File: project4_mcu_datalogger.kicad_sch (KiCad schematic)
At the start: 25 parts, among them U1 24LC1025, U2 24LC1025, U3 ATMEGA328P-AU, U4 DS1337S_T_R, Y1 32.768 KHz, Y2 16 MHz

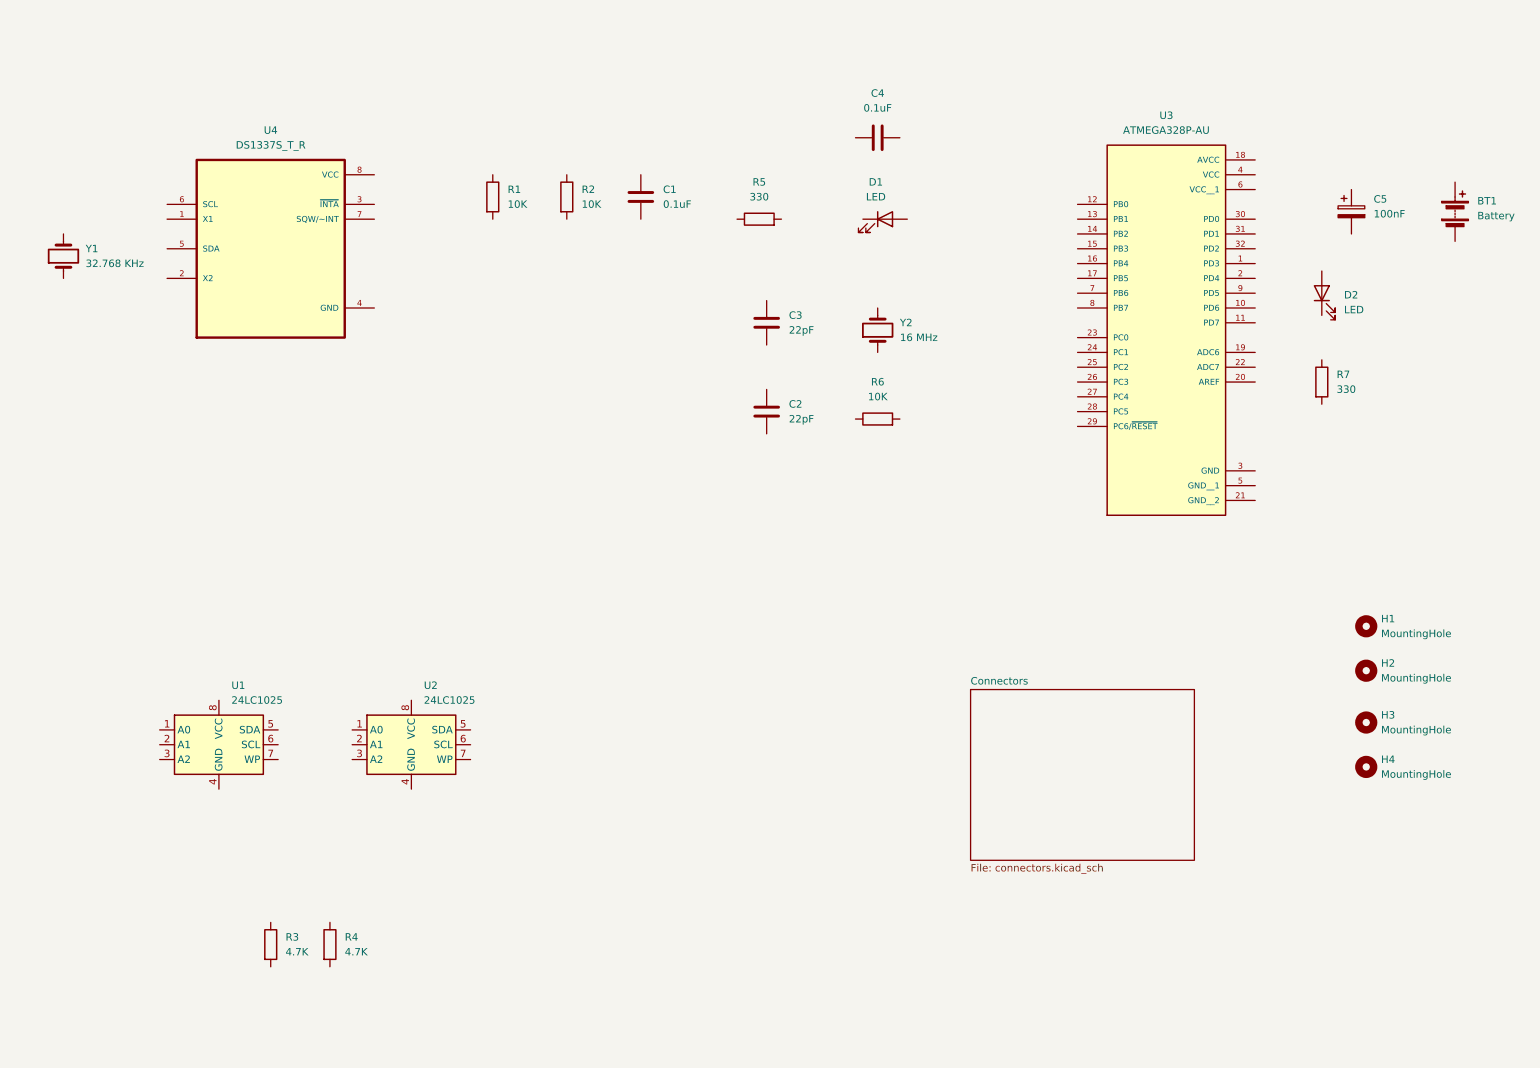
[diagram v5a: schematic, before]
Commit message: Completed wiring of main sheet
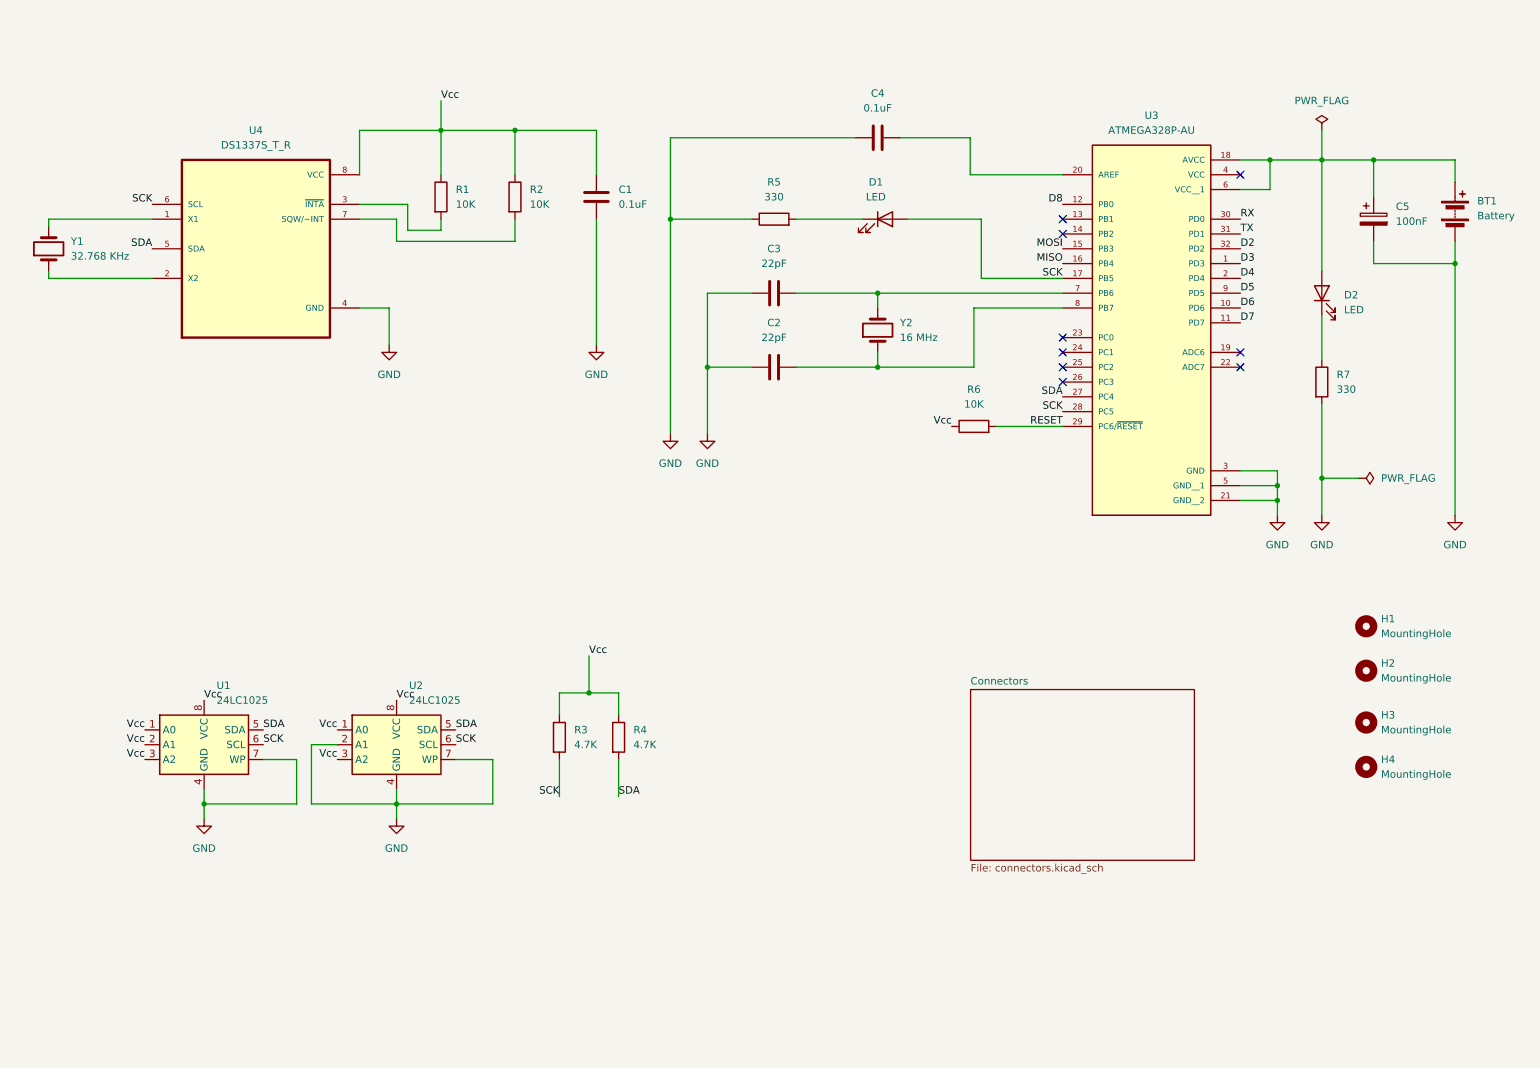
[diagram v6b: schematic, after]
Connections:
- net at R7.1: now also D2.1 (K)
- net GND: now reaches R7.2
- net GND: now also BT1.2 (-), C1.2, C2.1, C3.1, C4.1, C5.2, R5.1, U1.4 (GND), U1.7 (WP), U2.2 (A1), U2.4 (GND), U2.7 (WP), U3.21 (GND__2), U3.3 (GND), U3.5 (GND__1), U4.4 (GND)
- net Vcc: now reaches C1.1
- net Vcc: now also R1.1, R2.1, R3.1, R4.1, R6.1, U1.1 (A0), U1.2 (A1), U1.3 (A2), U1.8 (VCC), U2.1 (A0), U2.3 (A2), U2.8 (VCC), U4.8 (VCC)
- net at R5.2: now also D1.1 (K)
- net at BT1.1 (+): now also C5.1, D2.2 (A), U3.18 (AVCC), U3.6 (VCC__1)
- net at C2.2: now also U3.8 (PB7), Y2.1
- net at C4.2: now also U3.20 (AREF)
- net SDA: now reaches R4.2
- net SDA: now also U1.5 (SDA), U2.5 (SDA), U3.27 (PC4), U4.5 (SDA)
- net at C3.2: now also U3.7 (PB6), Y2.2
- net SCK: now reaches U1.6 (SCL)
- net SCK: now also D1.2 (A), R3.2, U2.6 (SCL), U3.17 (PB5), U3.28 (PC5), U4.6 (SCL)
- net at U4.1 (X1): now also Y1.2
- net at U4.2 (X2): now also Y1.1
- net at U4.3 (~{INTA}): now also R1.2
- net at U4.7 (SQW/~INT): now also R2.2
- net RESET: now reaches R6.2
- net RESET: now also U3.29 (PC6/~{RESET})
- net D3: now reaches U3.1 (PD3)
- net D6: now reaches U3.10 (PD6)
- net D7: now reaches U3.11 (PD7)
- net D8: now reaches U3.12 (PB0)
- net MOSI: now reaches U3.15 (PB3)
- net MISO: now reaches U3.16 (PB4)
- net D4: now reaches U3.2 (PD4)
- net RX: now reaches U3.30 (PD0)
- net TX: now reaches U3.31 (PD1)
- net D2: now reaches U3.32 (PD2)
- net D5: now reaches U3.9 (PD5)
- no-connect marks 0 -> 9
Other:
- moved on the sheet: C1, C2, C3, C5, R1, R2, R3, R4, R5, R6, U1, U2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

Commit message: Completed wiring in the second sheet
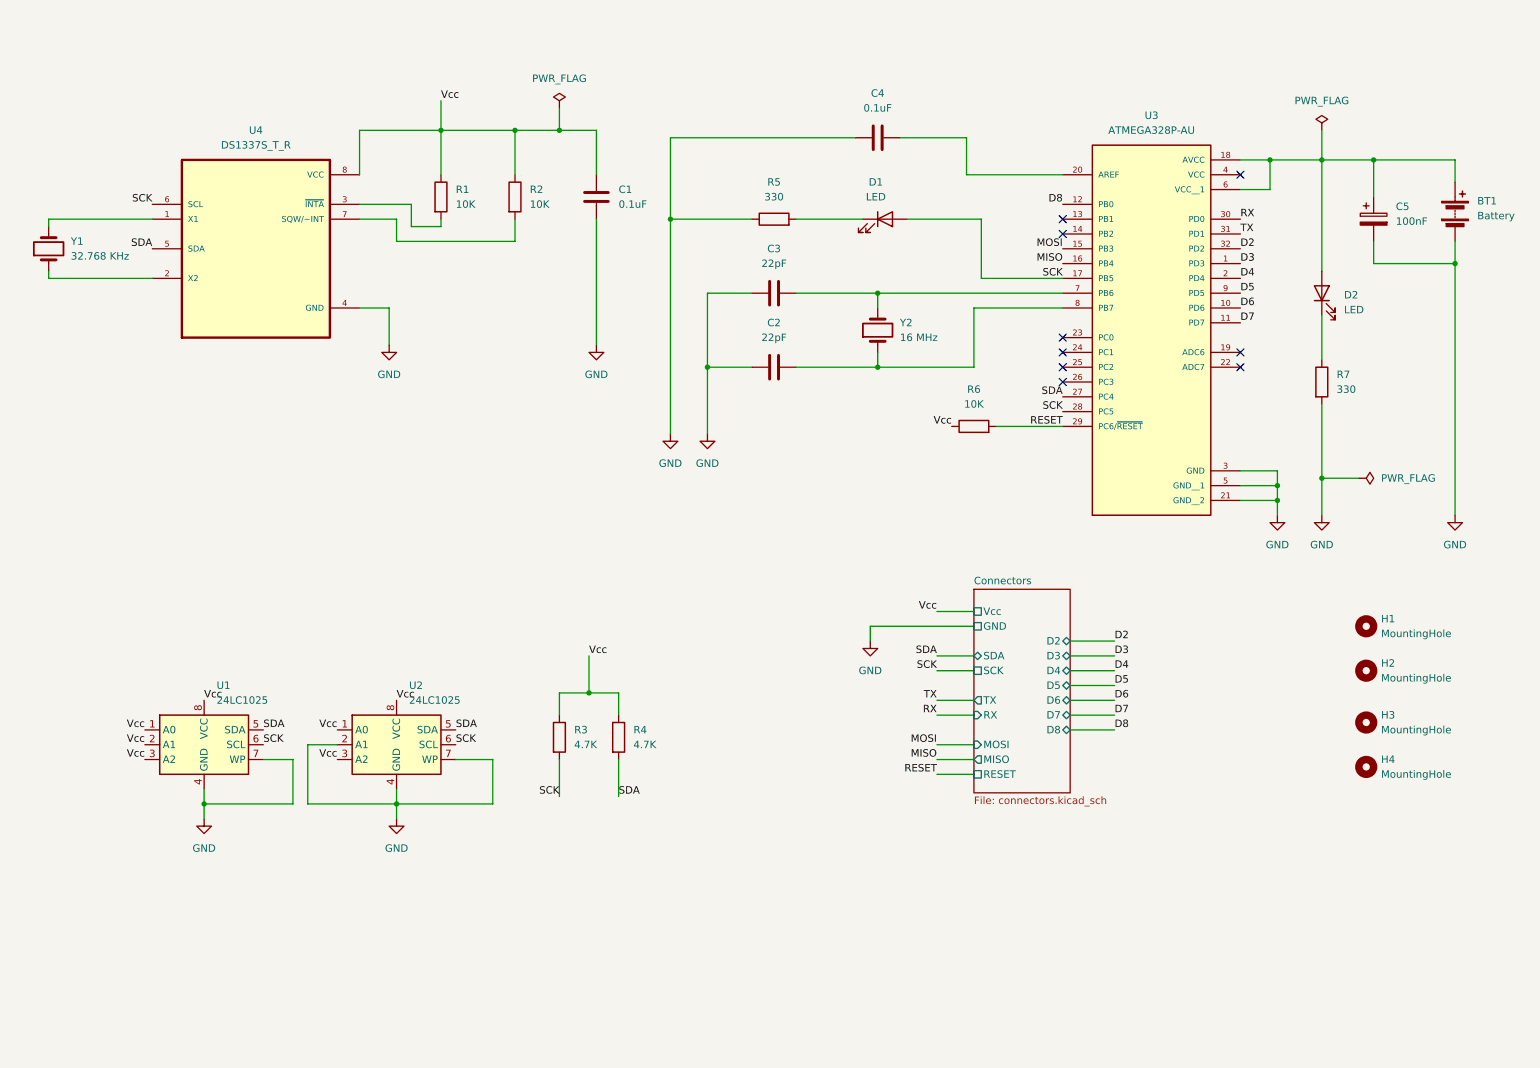
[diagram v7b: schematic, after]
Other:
- sheet Connectors ports: added D2, D3, D4, D5, D6, D7, D8, GND, MISO, MOSI, RESET, RX, SCK, SDA, TX, Vcc; removed none
